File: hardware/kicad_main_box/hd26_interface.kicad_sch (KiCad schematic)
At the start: 1 part, among them J1 DEUTSCH_DTM12_HEADER

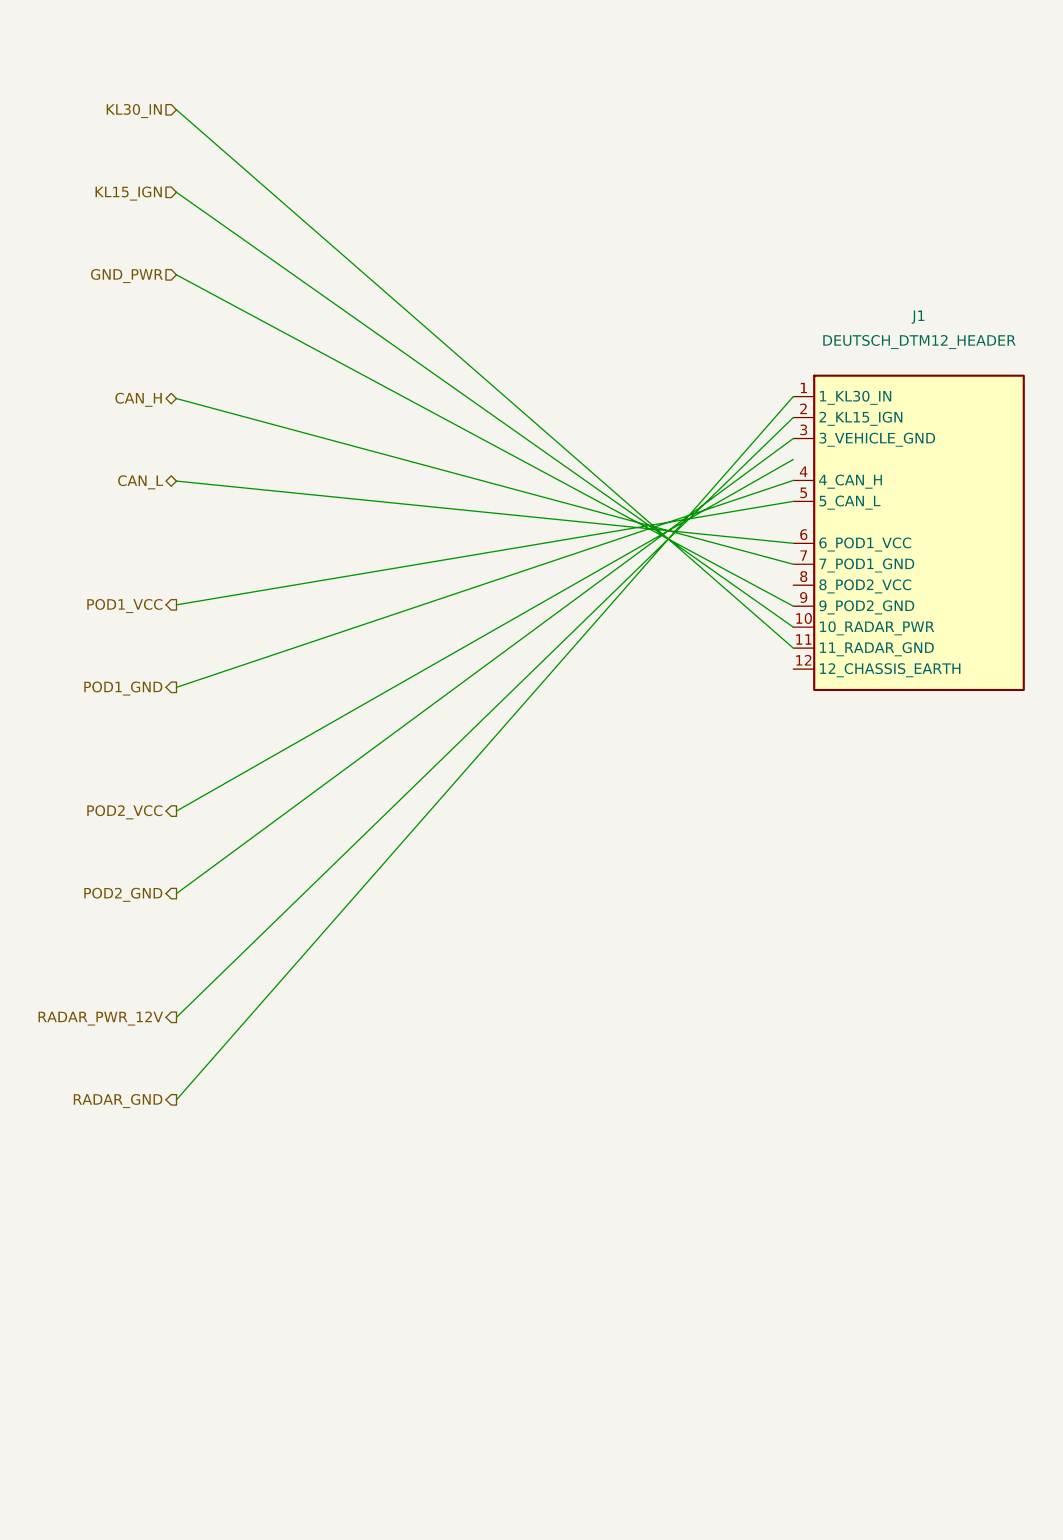
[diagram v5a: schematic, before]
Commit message: hardware(cartridge): move ES8388 audio codec to B.Cu bottom layer to eliminate overlaps and isolate from actuator MOSFETs
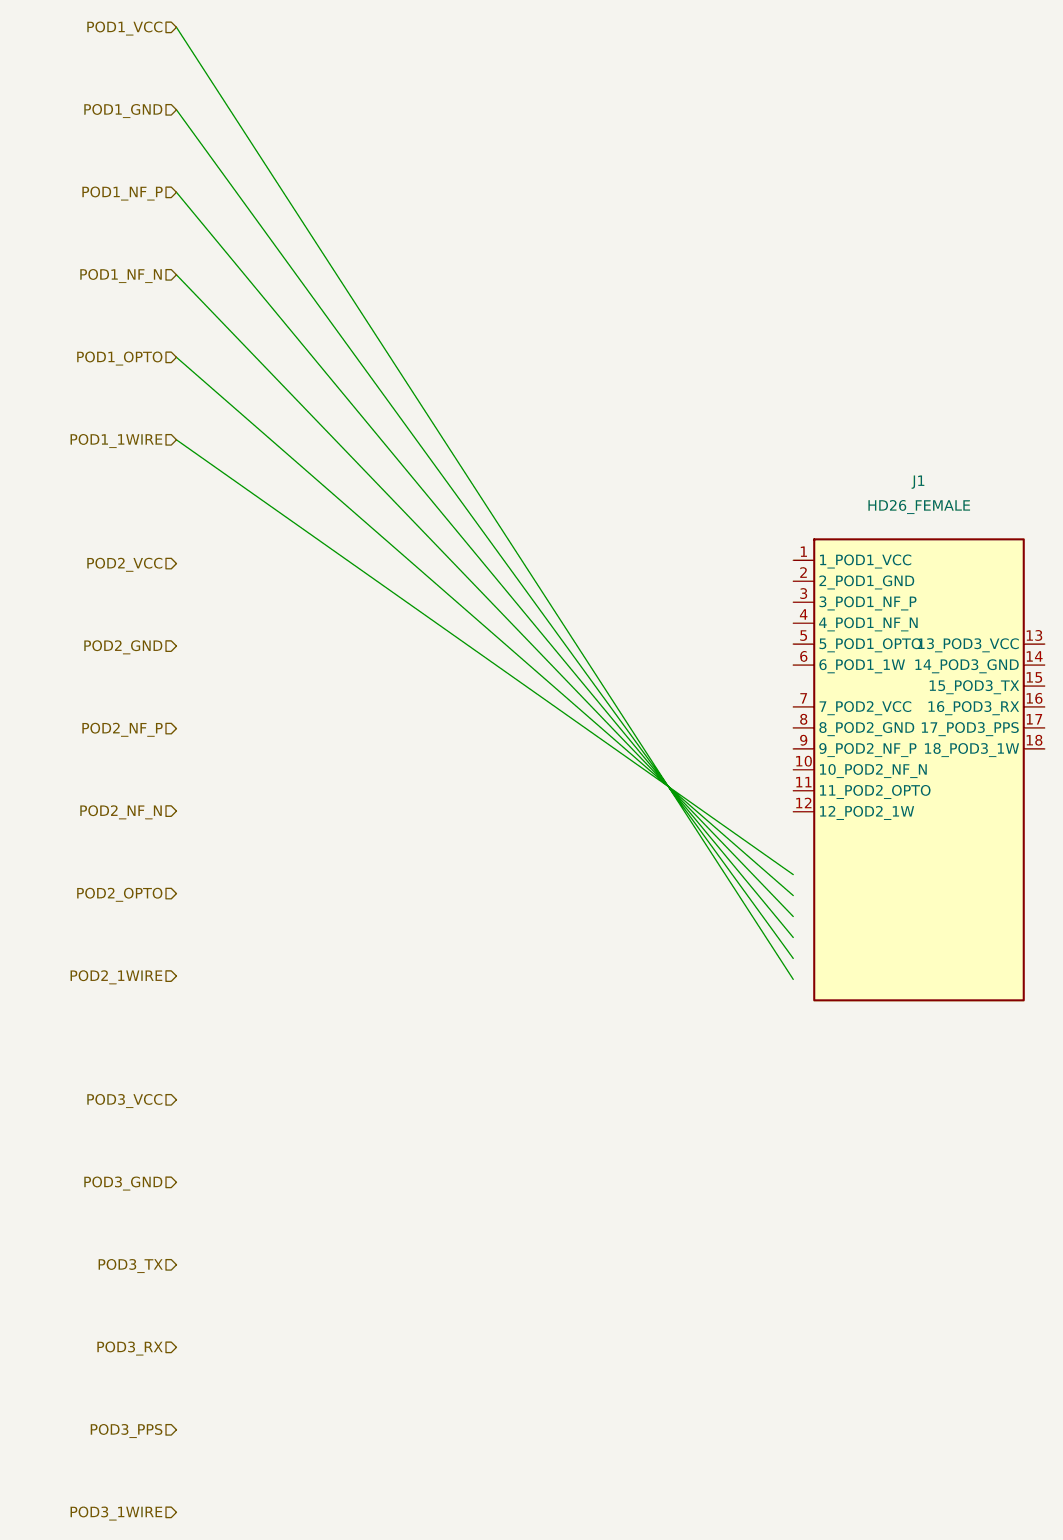
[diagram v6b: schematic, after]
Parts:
- J1: value DEUTSCH_DTM12_HEADER -> HD26_FEMALE; footprint Connector_IDC:IDC-Header_2x06_P2.54mm_Vertical -> Connector_IDC:IDC-Header_2x13_P2.54mm_Vertical; symbol Connector:Deutsch_DTM12_Male -> Connector:HD26_Female; LCSC C2934175 -> (none)
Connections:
- net POD1_GND: no longer J1.4 (4_CAN_H)
- net POD1_VCC: no longer J1.5 (5_CAN_L)
- net POD2_GND: no longer J1.3 (3_VEHICLE_GND)
- net CAN_H: no longer names the net of J1.7 (7_POD2_VCC)
- net CAN_L: no longer names the net of J1.6 (6_POD1_1W)
- net GND_PWR: no longer names the net of J1.9 (9_POD2_NF_P)
- net KL15_IGN: no longer names the net of J1.10 (10_POD2_NF_N)
- net KL30_IN: no longer names the net of J1.11 (11_POD2_OPTO)
- net RADAR_GND: no longer names the net of J1.1 (1_POD1_VCC)
- net RADAR_PWR_12V: no longer names the net of J1.2 (2_POD1_GND)
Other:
- title: OpenMotorBridge v8.5 / v9.0 - Deutsch DTM-12 Power & CAN Interface -> OpenMotorBridge v8.0 - HD26 Matrix-Schnittstelle & Bordnetz
